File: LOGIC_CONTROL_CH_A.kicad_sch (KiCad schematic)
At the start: 47 parts, among them IC1601 ${DEVICE}, IC1602 ${DEVICE}, IC1603 ${DEVICE}, IC1604 ${DEVICE}, IC1605 ${DEVICE}, IC1606 ${DEVICE}, IC1607 ${DEVICE}

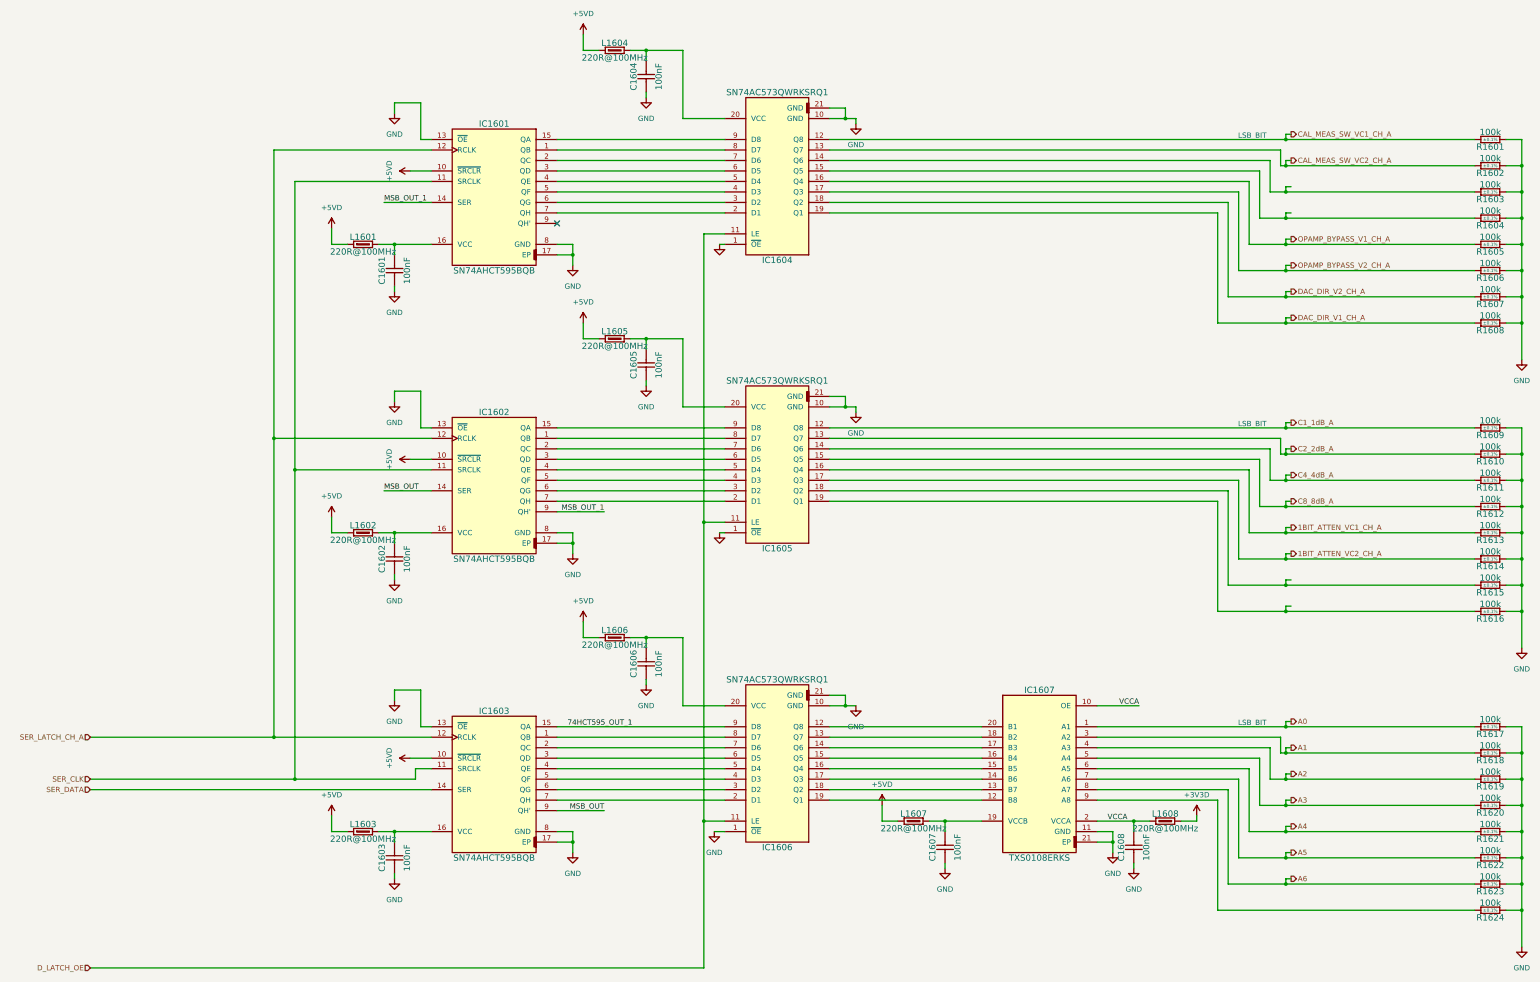
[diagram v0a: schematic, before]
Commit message: New channels topolgy added
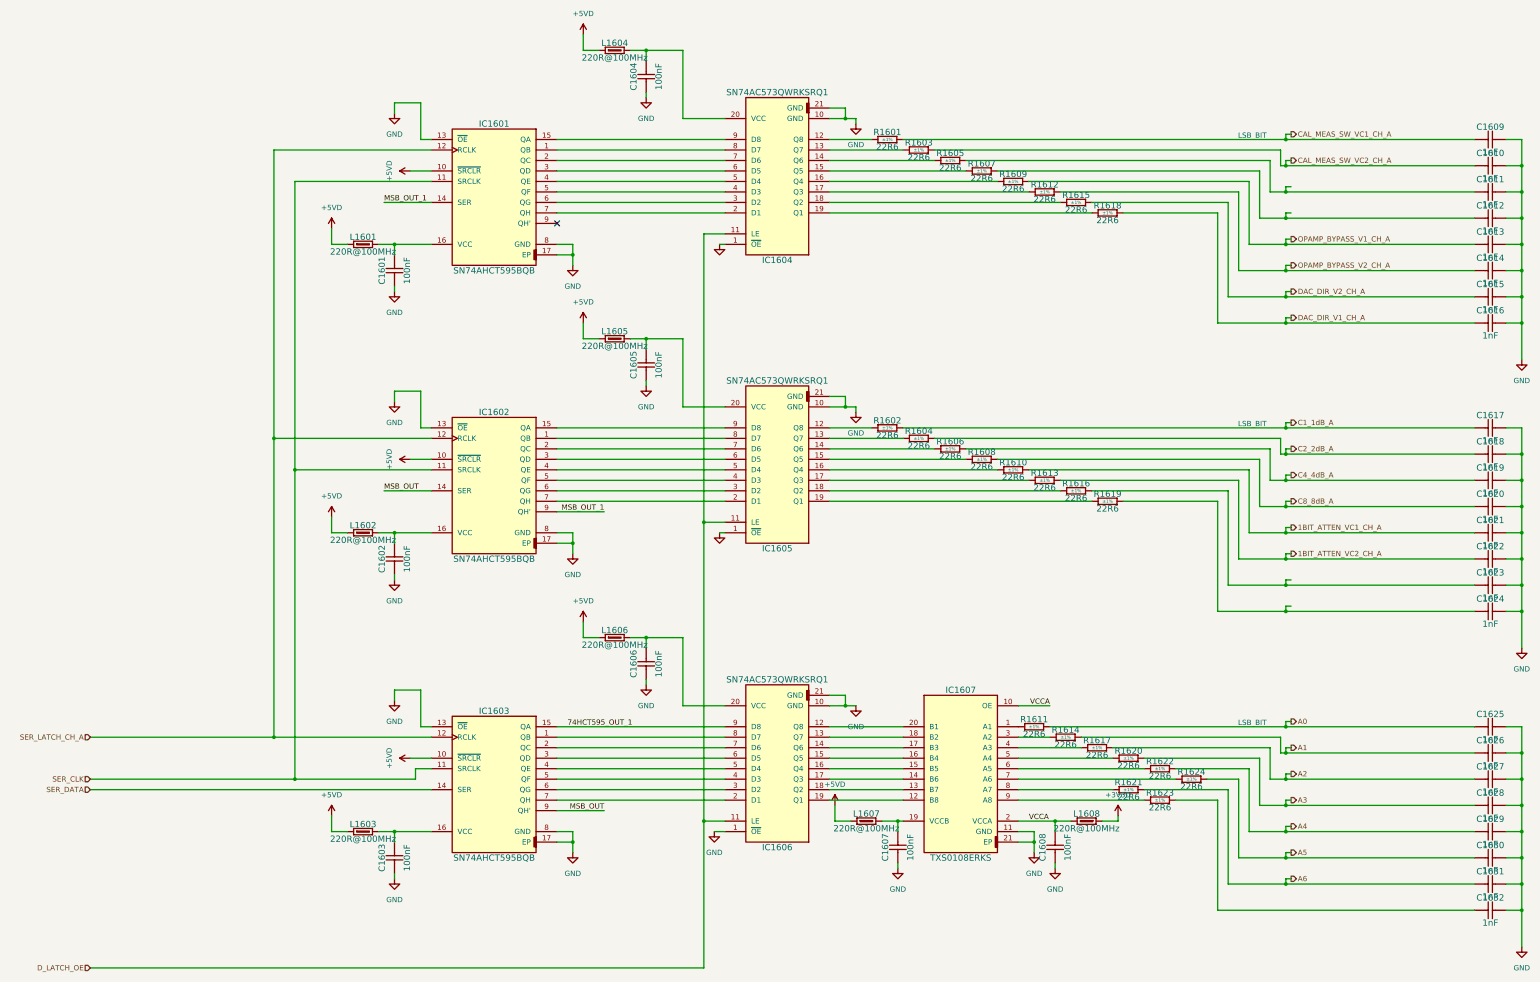
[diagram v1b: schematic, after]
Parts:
- removed R1601, R1602, R1603, R1604, R1605, R1606, R1607, R1608, R1609, R1610, R1611, R1612, R1613, R1614, R1615, R1616, R1617, R1618, R1619, R1620, R1621, R1622, R1623, R1624: 100k, Resistors SMD:RESC1005X35N, symbol CERN:Resistors SMD/R0402_10K_0.1%_0.063W_25PPM
- added C1609, C1610, C1611, C1612, C1613, C1614, C1615, C1616, C1617, C1618, C1619, C1620, C1621, C1622, C1623, C1624, C1625, C1626, C1627, C1628, C1629, C1630, C1631, C1632: 1nF, Capacitors SMD:CAPC1005X55N, symbol CERN:Capacitors SMD/CC0402_1NF_50V_5%_C0G
- added R1601, R1602, R1603, R1604, R1605, R1606, R1607, R1608, R1609, R1610, R1611, R1612, R1613, R1614, R1615, R1616, R1617, R1618, R1619, R1620, R1621, R1622, R1623, R1624: 22R6, Resistors SMD:RESC1005X40N, symbol CERN:Resistors SMD/R0402_22R6_1%_0.063W_100PPM
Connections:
- net 1BIT_ATTEN_VC1_CH_A: now also C1621.1, R1610.2; no longer IC1605.16 (Q4)
- net 1BIT_ATTEN_VC2_CH_A: now also C1622.1, R1613.2; no longer IC1605.17 (Q3)
- net A0: now also C1625.1, R1611.2; no longer IC1607.1 (A1)
- net A1: now also C1626.1, R1614.2; no longer IC1607.3 (A2)
- net A2: now also C1627.1, R1617.2; no longer IC1607.4 (A3)
- net A3: now also C1628.1, R1620.2; no longer IC1607.5 (A4)
- net A4: now also C1629.1, R1622.2; no longer IC1607.6 (A5)
- net A5: now also C1630.1, R1624.2; no longer IC1607.7 (A6)
- net A6: now also C1631.1, R1621.2; no longer IC1607.8 (A7)
- net C1_1dB_A: now also C1617.1, R1602.2; no longer IC1605.12 (Q8)
- net C2_2dB_A: now also C1618.1, R1604.2; no longer IC1605.13 (Q7)
- net C4_4dB_A: now also C1619.1, R1606.2; no longer IC1605.14 (Q6)
- net C8_8dB_A: now also C1620.1, R1608.2; no longer IC1605.15 (Q5)
- net CAL_MEAS_SW_VC1_CH_A: now also C1609.1, R1601.2; no longer IC1604.12 (Q8)
- net CAL_MEAS_SW_VC2_CH_A: now also C1610.1, R1603.2; no longer IC1604.13 (Q7)
- net DAC_DIR_V1_CH_A: now also C1616.1, R1618.2; no longer IC1604.19 (Q1)
- net DAC_DIR_V2_CH_A: now also C1615.1, R1615.2; no longer IC1604.18 (Q2)
- net GND: now also C1609.2, C1610.2, C1611.2, C1612.2, C1613.2, C1614.2, C1615.2, C1616.2, C1617.2, C1618.2, C1619.2, C1620.2, C1621.2, C1622.2, C1623.2, C1624.2, C1625.2, C1626.2, C1627.2, C1628.2, C1629.2, C1630.2, C1631.2, C1632.2
- net OPAMP_BYPASS_V1_CH_A: now also C1613.1, R1609.2; no longer IC1604.16 (Q4)
- net OPAMP_BYPASS_V2_CH_A: now also C1614.1, R1612.2; no longer IC1604.17 (Q3)
- net at IC1607.9 (A8): now also R1623.1
- net at IC1605.18 (Q2): now also R1616.1
- net at IC1605.19 (Q1): now also R1619.1
- net at IC1604.14 (Q6): now also R1605.1
- net at IC1604.15 (Q5): now also R1607.1
- new net: IC1607.3 (A2), R1614.1
- new net: C1611.1, R1605.2
- new net: C1624.1, R1619.2
- new net: IC1607.6 (A5), R1622.1
- new net: IC1607.5 (A4), R1620.1
- new net: C1623.1, R1616.2
- new net: IC1604.19 (Q1), R1618.1
- new net: IC1607.4 (A3), R1617.1
- new net: IC1607.1 (A1), R1611.1
- new net: IC1604.16 (Q4), R1609.1
- new net: IC1605.12 (Q8), R1602.1
- new net: IC1605.13 (Q7), R1604.1
- new net: IC1605.14 (Q6), R1606.1
- new net: IC1605.15 (Q5), R1608.1
- new net: IC1605.16 (Q4), R1610.1
- new net: IC1605.17 (Q3), R1613.1
- new net: C1632.1, R1623.2
- new net: C1612.1, R1607.2
- new net: IC1604.12 (Q8), R1601.1
- new net: IC1607.7 (A6), R1624.1
- new net: IC1607.8 (A7), R1621.1
- new net: IC1604.18 (Q2), R1615.1
- new net: IC1604.13 (Q7), R1603.1
- new net: IC1604.17 (Q3), R1612.1
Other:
- moved on the sheet: C1607, C1608, IC1607, L1607, L1608
